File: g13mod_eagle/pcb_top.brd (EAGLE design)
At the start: 85.2 x 17.3 mm, 0 parts

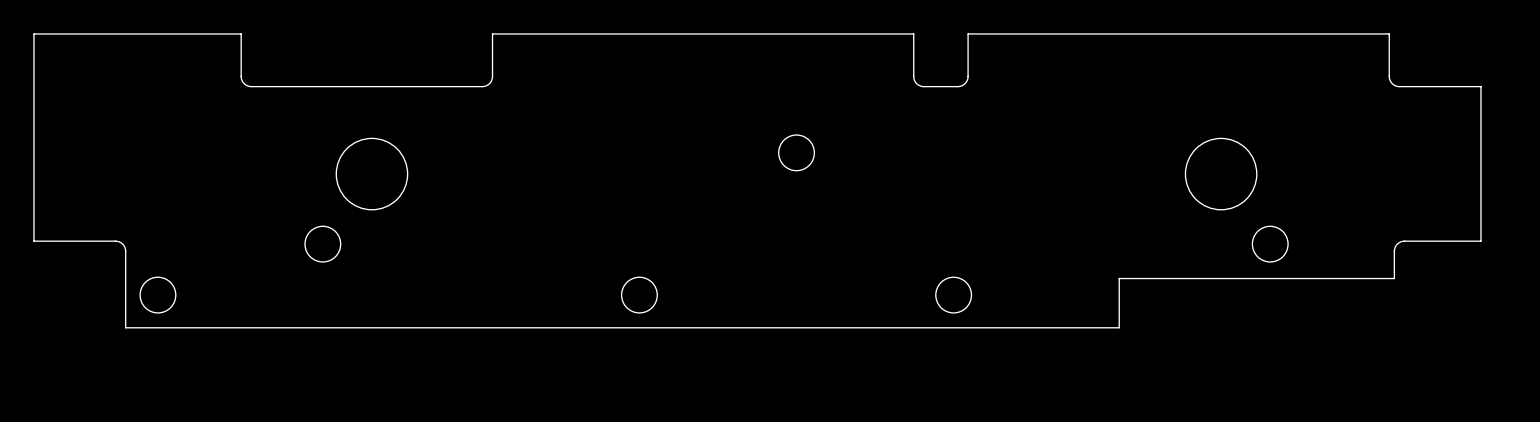
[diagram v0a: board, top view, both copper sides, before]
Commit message: Add switches
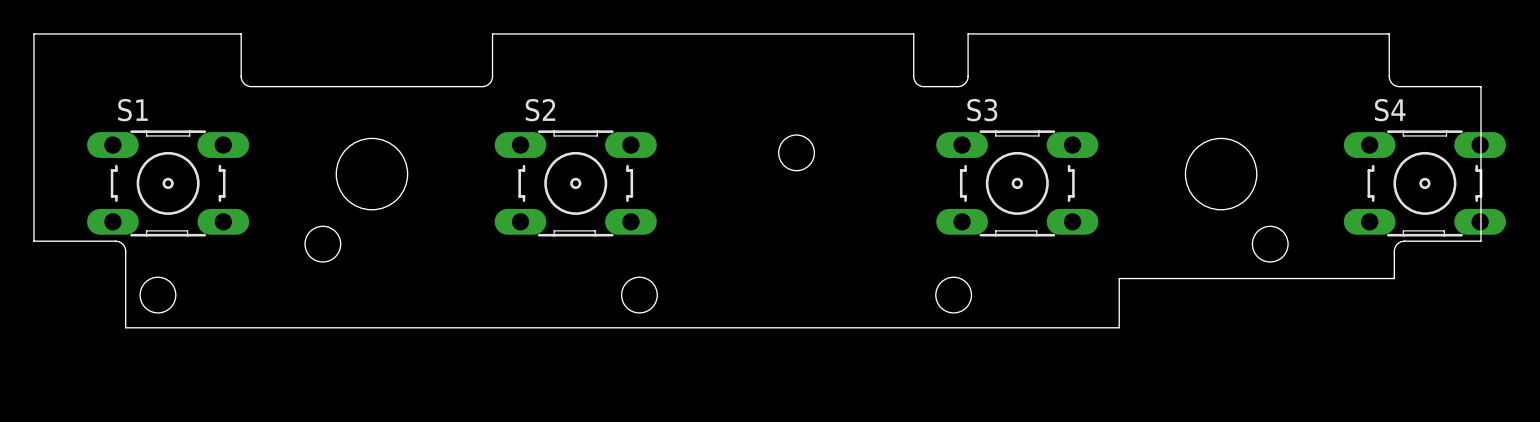
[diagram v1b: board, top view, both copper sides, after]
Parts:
- added S1, S2, S3, S4: (no value), switch-omron:B3F-10XX
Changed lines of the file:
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@@
 <setting verticaltext="up"/>
 </settings>
-<grid distance="50" unitdist="mil" unit="mil" style="lines" multiple="1" display="no" altdistance="5" altunitdist="mil" altunit="mil"/>
+<grid distance="50" unitdist="mil" unit="mm" style="lines" multiple="1" display="no" altdistance="5" altunitdist="mil" altunit="mm"/>
 <layers>
 <layer number="1" name="Top" color="4" fill="1" visible="yes" active="yes"/>
+<layer number="2" name="Route2" color="1" fill="3" visible="no" active="no"/>
+<layer number="3" name="Route3" color="4" fill="3" visible="no" active="no"/>
+<layer number="4" name="Route4" color="1" fill="4" visible="no" active="no"/>
+<layer number="5" name="Route5" color="4" fill="4" visible="no" active="no"/>
+<layer number="6" name="Route6" color="1" fill="8" visible="no" active="no"/>
+<layer number="7" name="Route7" color="4" fill="8" visible="no" active="no"/>
+<layer number="8" name="Route8" color="1" fill="2" visible="no" active="no"/>
+<layer number="9" name="Route9" color="4" fill="2" visible="no" active="no"/>
+<layer number="10" name="Route10" color="1" fill="7" visible="no" active="no"/>
+<layer number="11" name="Route11" color="4" fill="7" visible="no" active="no"/>
+<layer number="12" name="Route12" color="1" fill="5" visible="no" active="no"/>
+<layer number="13" name="Route13" color="4" fill="5" visible="no" active="no"/>
+<layer number="14" name="Route14" color="1" fill="6" visible="no" active="no"/>
+<layer number="15" name="Route15" color="4" fill="6" visible="no" active="no"/>
 <layer number="16" name="Bottom" color="1" fill="1" visible="yes" active="yes"/>
 <layer number="17" name="Pads" color="2" fill="1" visible="yes" active="yes"/>
@@
 </autorouter>
 <elements>
+<element name="S1" library="switch-omron" library_urn="urn:adsk.eagle:library:377" package="B3F-10XX" package3d_urn="urn:adsk.eagle:package:27496/1" value="" x="-37" y="3.552" smashed="yes">
+<attribute name="MF" value="" x="-37" y="3.552" size="1.778" layer="27" display="off"/>
+<attribute name="MPN" value="B3F-1000" x="-37" y="3.552" size="1.778" layer="27" display="off"/>
+<attribute name="NAME" x="-40.048" y="7.235" size="1.27" layer="25" ratio="10"/>
+<attribute name="OC_FARNELL" value="176432" x="-37" y="3.552" size="1.778" layer="27" display="off"/>
+<attribute name="OC_NEWARK" value="36M3542" x="-37" y="3.552" size="1.778" layer="27" display="off"/>
+<attribute name="POPULARITY" value="72" x="-37" y="3.552" size="1.778" layer="27" display="off"/>
+<attribute name="VALUE" x="-40.048" y="-1.528" size="1.27" layer="27" ratio="10"/>
+</element>
+<element name="S2" library="switch-omron" library_urn="urn:adsk.eagle:library:377" package="B3F-10XX" package3d_urn="urn:adsk.eagle:package:27496/1" value="" x="-13" y="3.552" smashed="yes">
+<attribute name="MF" value="" x="-13" y="3.552" size="1.778" layer="27" display="off"/>
+<attribute name="MPN" value="B3F-1000" x="-13" y="3.552" size="1.778" layer="27" display="off"/>
+<attribute name="NAME" x="-16.048" y="7.235" size="1.27" layer="25" ratio="10"/>
+<attribute name="OC_FARNELL" value="176432" x="-13" y="3.552" size="1.778" layer="27" display="off"/>
+<attribute name="OC_NEWARK" value="36M3542" x="-13" y="3.552" size="1.778" layer="27" display="off"/>
+<attribute name="POPULARITY" value="72" x="-13" y="3.552" size="1.778" layer="27" display="off"/>
+<attribute name="VALUE" x="-16.048" y="-1.528" size="1.27" layer="27" ratio="10"/>
+</element>
+<element name="S3" library="switch-omron" library_urn="urn:adsk.eagle:library:377" package="B3F-10XX" package3d_urn="urn:adsk.eagle:package:27496/1" value="" x="13" y="3.552" smashed="yes">
+<attribute name="MF" value="" x="13" y="3.552" size="1.778" layer="27" display="off"/>
+<attribute name="MPN" value="B3F-1000" x="13" y="3.552" size="1.778" layer="27" display="off"/>
+<attribute name="NAME" x="9.952" y="7.235" size="1.27" layer="25" ratio="10"/>
+<attribute name="OC_FARNELL" value="176432" x="13" y="3.552" size="1.778" layer="27" display="off"/>
+<attribute name="OC_NEWARK" value="36M3542" x="13" y="3.552" size="1.778" layer="27" display="off"/>
+<attribute name="POPULARITY" value="72" x="13" y="3.552" size="1.778" layer="27" display="off"/>
+<attribute name="VALUE" x="9.952" y="-1.528" size="1.27" layer="27" ratio="10"/>
+</element>
+<element name="S4" library="switch-omron" library_urn="urn:adsk.eagle:library:377" package="B3F-10XX" package3d_urn="urn:adsk.eagle:package:27496/1" value="" x="37" y="3.552" smashed="yes">
+<attribute name="MF" value="" x="37" y="3.552" size="1.778" layer="27" display="off"/>
+<attribute name="MPN" value="B3F-1000" x="37" y="3.552" size="1.778" layer="27" display="off"/>
+<attribute name="NAME" x="33.952" y="7.235" size="1.27" layer="25" ratio="10"/>
+<attribute name="OC_FARNELL" value="176432" x="37" y="3.552" size="1.778" layer="27" display="off"/>
+<attribute name="OC_NEWARK" value="36M3542" x="37" y="3.552" size="1.778" layer="27" display="off"/>
+<attribute name="POPULARITY" value="72" x="37" y="3.552" size="1.778" layer="27" display="off"/>
+<attribute name="VALUE" x="33.952" y="-1.528" size="1.27" layer="27" ratio="10"/>
+</element>
 </elements>
 <signals>
@@
 </board>
 </drawing>
+<compatibility>
+<note version="8.2" severity="warning">
+Since Version 8.2, EAGLE supports online libraries. The ids
+of those online libraries will not be understood (or retained)
+with this version.
+</note>
+<note version="8.3" severity="warning">
+Since Version 8.3, EAGLE supports URNs for individual library
+assets (packages, symbols, and devices). The URNs of those assets
+will not be understood (or retained) with this version.
+</note>
+<note version="8.3" severity="warning">
+Since Version 8.3, EAGLE supports the association of 3D packages
+with devices in libraries, schematics, and board files. Those 3D
+packages will not be understood (or retained) with this version.
+</note>
+</compatibility>
 </eagle>

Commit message: wiring
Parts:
- removed S1, S2, S3, S4: (no value), switch-omron:B3F-10XX
- added CN6: (no value), pinhead-half-pitch:THROUHOLE18
- added CN7: (no value), pinhead-half-pitch:THROUHOLE15
- added JP2, JP3: (no value), pinhead-half-pitch:THROUHOLE05
- added JP4, JP7: (no value), pinhead-half-pitch:THROUHOLE04
- added JP5, JP6: (no value), pinhead-half-pitch:THROUHOLE12
- added LED1, LED2, LED3, LED4: (no value), led:CHIPLED_1206
- added M1, M2, M3, MR: (no value), switch-omron:B3F-10XX
- added R1, R2, R3, R4: (no value), rcl:R0603
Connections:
- new net CN6_1: CN6.1, M3.2
- new net CN6_10: CN6.10, JP5.5
- new net CN6_11: CN6.11, JP5.6
- new net CN6_12: CN6.12, M1.2
- new net CN6_13: CN6.13, JP5.7
- new net CN6_14: CN6.14, JP5.8
- new net CN6_15: CN6.15, JP5.9, M2.2
- new net CN6_16: CN6.16, JP5.10
- new net CN6_17: CN6.17, JP5.11
- new net CN6_18: CN6.18, JP5.12
- new net CN6_2: CN6.2, MR.2
- new net CN6_3: CN6.3, JP6.10
- new net CN6_4: CN6.4, JP6.11
- new net CN6_5: CN6.5, JP6.12
- new net CN6_6: CN6.6, JP5.1
- new net CN6_7: CN6.7, JP5.2
- new net CN6_8: CN6.8, JP5.3
- new net CN6_9: CN6.9, JP5.4
- new net CN7_1: CN7.1, JP2.1
- new net CN7_10: CN7.10, JP6.4
- new net CN7_11: CN7.11, JP6.5
- new net CN7_12: CN7.12, JP6.6
- new net CN7_13: CN7.13, JP6.7
- new net CN7_14: CN7.14, JP6.8
- new net CN7_15: CN7.15, JP6.9
- new net CN7_2: CN7.2, JP2.2
- new net CN7_3: CN7.3, JP2.3
- new net CN7_4: CN7.4, JP2.4
- new net CN7_5: CN7.5, M1.4, M2.4, MR.4
- new net CN7_6: CN7.6, JP2.5
- new net CN7_7: CN7.7, JP6.1, M3.4
- new net CN7_8: CN7.8, JP6.2
- new net CN7_9: CN7.9, JP6.3
- new net LED_M1: JP3.4, R1.1
- new net LED_M2: JP3.3, R2.1
- new net LED_M3: JP3.2, R3.1
- new net LED_MR: JP3.1, R4.1
- new net N$1: JP4.1, JP7.1
- new net N$2: JP4.2, JP7.2
- new net N$3: JP4.3, JP7.3
- new net N$4: JP4.4, JP7.4
- new net N$5: JP3.5, LED1.A, LED2.A, LED3.A, LED4.A
- new net N$6: LED1.C, R1.2
- new net N$7: LED2.C, R2.2
- new net N$8: LED3.C, R3.2
- new net N$9: LED4.C, R4.2
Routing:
- net CN7_5: track 0.00 -> 94.5 mm, vias 0 -> 2
- net N$5: track 0.00 -> 91.4 mm, vias 0 -> 5
- net LED_MR: track 0.00 -> 82.5 mm
- net LED_M3: track 0.00 -> 55.7 mm
- net CN6_2: track 0.00 -> 44.4 mm
- net LED_M2: track 0.00 -> 40.3 mm
- net CN7_10: track 0.00 -> 28.9 mm
- net CN7_9: track 0.00 -> 28.9 mm
- net CN7_8: track 0.00 -> 28.8 mm
- net CN7_7: track 0.00 -> 28.6 mm, vias 0 -> 3
- net CN6_12: track 0.00 -> 28.2 mm, vias 0 -> 2
- net CN7_11: track 0.00 -> 27.0 mm
- net CN7_12: track 0.00 -> 26.6 mm
- net CN7_13: track 0.00 -> 26.2 mm
- net CN7_14: track 0.00 -> 25.9 mm
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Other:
- outline, holes or cut-outs redrawn

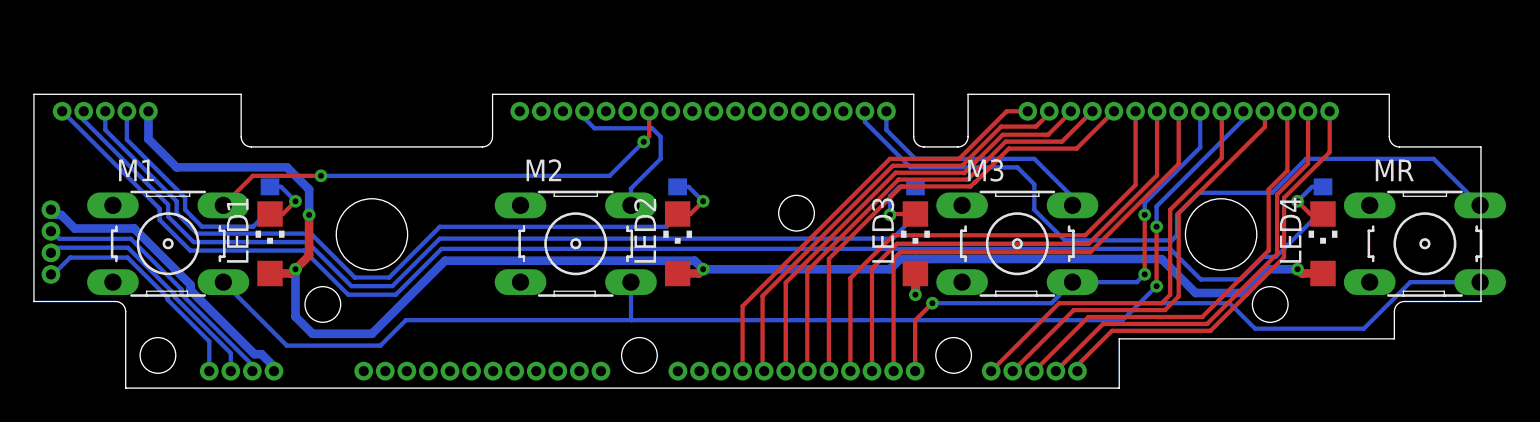
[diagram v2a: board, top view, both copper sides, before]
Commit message: wiring top pcb
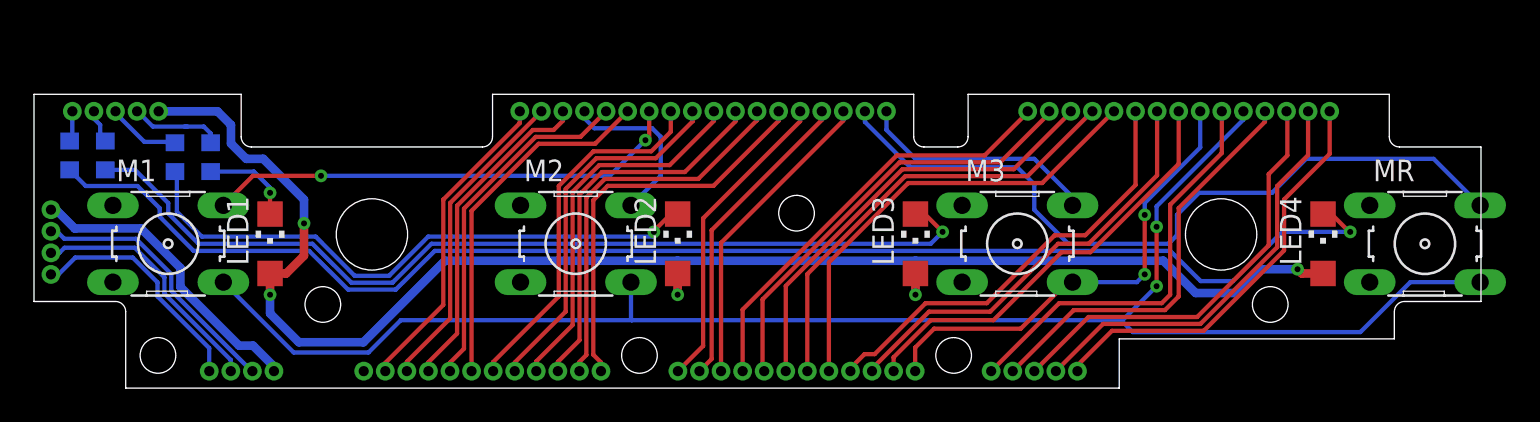
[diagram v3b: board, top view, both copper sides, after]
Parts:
- moved R4 73.8 mm to (-42.8, 5.20), turned to 270 degrees
- moved R3 47.8 mm to (-40.7, 5.20), turned to 270 degrees
- moved R2 29.7 mm to (-36.6, 5.10), turned to 270 degrees
- moved R1 4.36 mm to (-34.5, 5.10), turned to 270 degrees
- moved JP3 0.60 mm to (-40.1, 7.80)
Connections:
- net CN6_15: no longer JP5.9
- net CN6_16: now also JP5.9; no longer JP5.10
- net CN6_17: now also JP5.10; no longer JP5.11
- net CN6_18: now also JP5.11; no longer JP5.12
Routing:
- net LED_MR: track 82.5 -> 1.82 mm
- net N$9: track 3.66 -> 83.5 mm
- net LED_M3: track 55.7 -> 2.13 mm
- net N$8: track 4.53 -> 55.7 mm
- net LED_M2: track 40.3 -> 4.77 mm
- net N$7: track 3.66 -> 35.2 mm
- net CN6_6: track 0.00 -> 23.7 mm
- net CN6_7: track 0.00 -> 22.9 mm
- net CN6_8: track 0.00 -> 22.5 mm
- net CN6_9: track 0.00 -> 22.1 mm
- net CN6_10: track 0.00 -> 21.7 mm
- net CN6_11: track 0.00 -> 21.6 mm
- net CN6_13: track 0.00 -> 21.1 mm
- net CN6_14: track 0.00 -> 20.7 mm
- net CN6_16: track 0.00 -> 19.3 mm
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
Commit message: Edit connector
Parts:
- removed JP5, JP6: (no value), pinhead-half-pitch:THROUHOLE12
- added JP1: (no value), pinhead-half-pitch:THROUHOLE06
- added JP8: (no value), pinhead-half-pitch:THROUHOLE11
- JP2: device pinhead-half-pitch:THROUHOLE05 -> pinhead-half-pitch:THROUHOLE11
- moved JP2 14.0 mm to (0.00, -7.50)
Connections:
- net CN6_10: now also JP8.5; no longer JP5.5
- net CN6_11: now also JP8.6; no longer JP5.6
- net CN6_13: now also JP8.7; no longer JP5.7
- net CN6_14: now also JP8.8; no longer JP5.8
- net CN6_16: now also JP8.9; no longer JP5.9
- net CN6_17: now also JP8.10; no longer JP5.10
- net CN6_18: now also JP8.11; no longer JP5.11
- net CN6_3: now also JP2.9; no longer JP6.10
- net CN6_4: now also JP2.10; no longer JP6.11
- net CN6_5: now also JP2.11; no longer JP6.12
- net CN6_6: now also JP8.1; no longer JP5.1
- net CN6_7: now also JP8.2; no longer JP5.2
- net CN6_8: now also JP8.3; no longer JP5.3
- net CN6_9: now also JP8.4; no longer JP5.4
- net CN7_1: now also JP1.1; no longer JP2.1
- net CN7_10: now also JP2.3; no longer JP6.4
- net CN7_11: now also JP2.4; no longer JP6.5
- net CN7_12: now also JP2.5; no longer JP6.6
- net CN7_13: now also JP2.6; no longer JP6.7
- net CN7_14: now also JP2.7; no longer JP6.8
- net CN7_15: now also JP2.8; no longer JP6.9
- net CN7_2: now also JP1.2; no longer JP2.2
- net CN7_3: now also JP1.3; no longer JP2.3
- net CN7_4: now also JP1.4; no longer JP2.4
- net CN7_6: now also JP1.5; no longer JP2.5
- net CN7_7: now also JP1.6; no longer JP6.1
- net CN7_8: now also JP2.1; no longer JP6.2
- net CN7_9: now also JP2.2; no longer JP6.3
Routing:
- net CN7_7: track 27.6 -> 22.5 mm
- net CN7_4: track 24.6 -> 23.5 mm
- net CN7_3: track 25.2 -> 24.1 mm
- net CN7_6: track 24.7 -> 23.6 mm
- net CN7_2: track 24.8 -> 24.0 mm
- net CN7_1: track 24.6 -> 23.9 mm
- net CN6_11: track 21.6 -> 22.3 mm
- net CN7_10: track 25.8 -> 25.2 mm

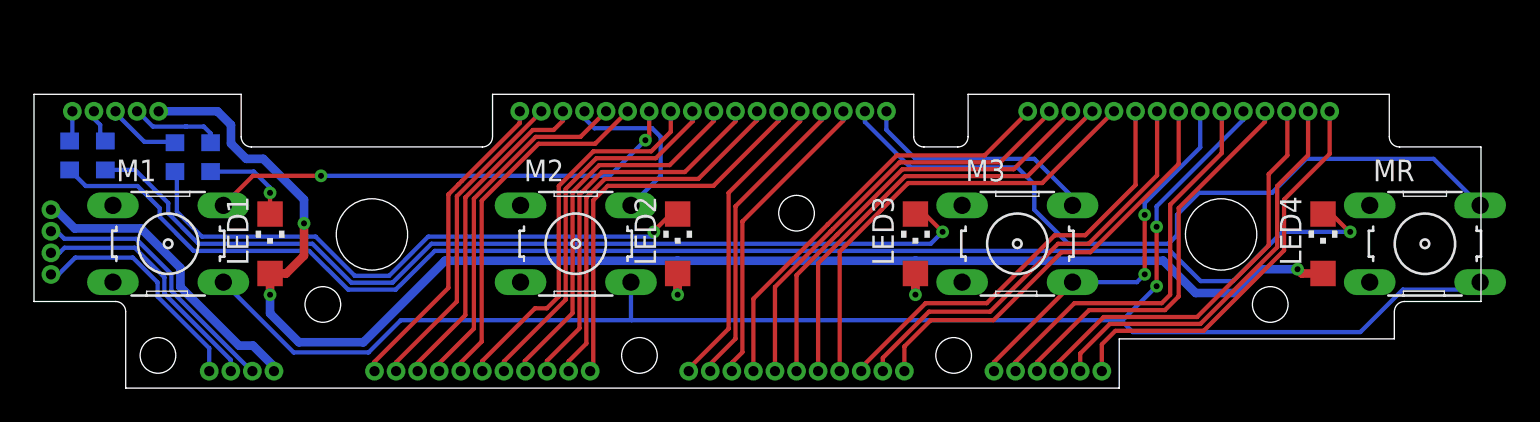
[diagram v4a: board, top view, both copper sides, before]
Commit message: wiring middle pcb
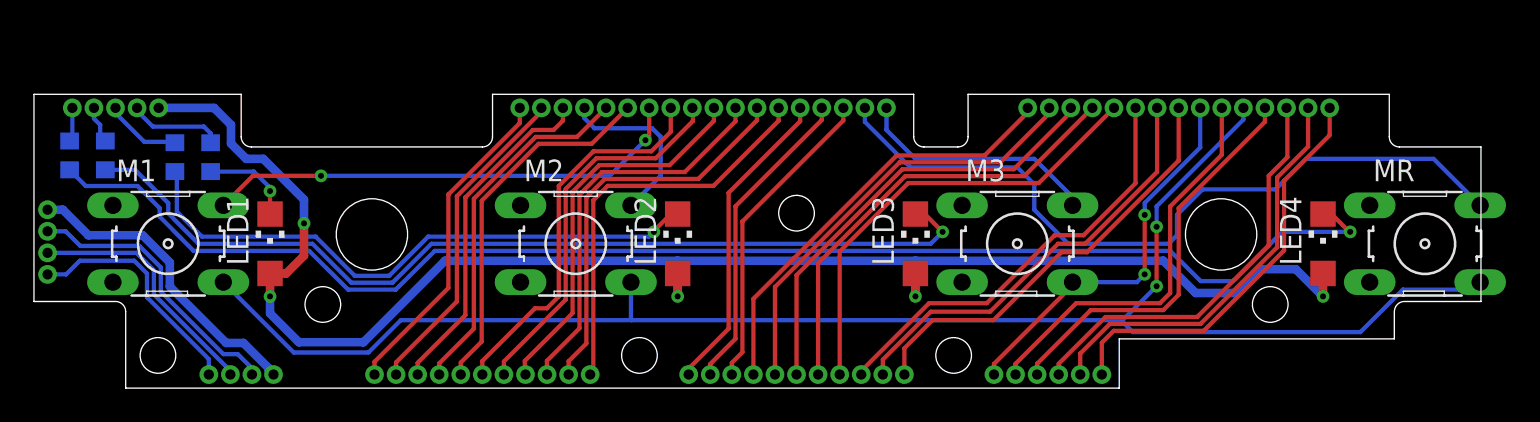
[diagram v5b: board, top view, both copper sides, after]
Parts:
- moved JP7 0.20 mm to (-32.7, -7.70), turned to 180 degrees
- moved JP4 0.20 mm to (-44.1, 0.10), turned to 270 degrees
- moved CN6 0.20 mm to (-5.50, 8.00)
- moved CN7 0.20 mm to (22.5, 8.00)
- moved JP1 0.20 mm to (14.8, -7.70)
- moved JP2 0.20 mm to (0.00, -7.70)
- moved JP3 0.20 mm to (-40.1, 8.00)
- moved JP8 0.20 mm to (-18.5, -7.70)
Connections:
- net N$1 renamed V
- net N$2 renamed G
- net N$3 renamed R
- net N$4 renamed B
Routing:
- net V: track 13.8 -> 18.2 mm
- net B: track 17.9 -> 14.0 mm
- net N$5: track 92.1 -> 94.5 mm
- net G: track 14.7 -> 16.6 mm
- net R: track 15.8 -> 14.7 mm

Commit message: Edit width
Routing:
- net CN6_15: track 10.3 -> 6.87 mm
- net CN7_10: track 25.4 -> 26.6 mm
- net CN6_12: track 28.5 -> 27.7 mm
- net CN7_9: track 25.4 -> 26.1 mm
- net CN6_2: track 44.8 -> 44.1 mm
- net CN6_17: track 19.2 -> 19.8 mm
- net CN7_13: track 26.2 -> 26.8 mm
- net CN7_15: track 25.4 -> 26.0 mm
- net CN7_14: track 25.9 -> 26.4 mm
- net CN7_11: track 26.9 -> 27.5 mm
- net CN7_12: track 26.5 -> 27.1 mm
